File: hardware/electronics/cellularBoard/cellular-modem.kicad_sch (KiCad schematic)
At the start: 24 parts, among them Q1 DMG1013TQ-7, U4 OPA344, U5 SARA-R422S-01B

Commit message: started on schematics
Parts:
- removed U5: SARA-R422S-01B, DSE-RF-Receivers:ZED-F9P-04B_UBL, symbol DS-RF-Tranceivers-and-Modems:SARA-R422S-01B
- added U2: LEXI-R520, symbol lib_sch:LEXI-R520
- added U3: LM51571-Q1, symbol lib_sch:LM51571-Q1
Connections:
- net VCC: now also U2.40 (VCC), U2.41 (VCC), U2.42 (VCC)
- net VSS: now also U2.1 (GND), U2.100 (GND), U2.101 (GND), U2.102 (GND), U2.103 (GND), U2.104 (GND), U2.105 (GND), U2.106 (GND), U2.109 (GND), U2.110 (GND), U2.111 (GND), U2.112 (GND), U2.113 (GND), U2.114 (GND), U2.115 (GND), U2.116 (GND), U2.117 (GND), U2.118 (GND), U2.119 (GND), U2.120 (GND), U2.121 (GND), U2.122 (GND), U2.123 (GND), U2.124 (GND), U2.125 (GND), U2.126 (GND), U2.127 (GND), U2.128 (GND), U2.129 (GND), U2.130 (GND), U2.131 (GND), U2.132 (GND), U2.133 (GND), U2.3 (GND), U2.50 (GND), U2.52 (GND), U2.53 (GND), U2.56 (GND), U2.57 (GND), U2.58 (GND), U2.59 (GND), U2.60 (GND), U2.61 (GND), U2.64 (GND), U2.65 (GND), U2.66 (GND), U2.67 (GND), U2.68 (GND), U2.69 (GND), U2.70 (GND), U2.73 (GND), U2.74 (GND), U2.75 (GND), U2.76 (GND), U2.77 (GND), U2.78 (GND), U2.79 (GND), U2.82 (GND), U2.83 (GND), U2.84 (GND), U2.85 (GND), U2.86 (GND), U2.87 (GND), U2.88 (GND), U2.91 (GND), U2.92 (GND), U2.93 (GND), U2.94 (GND), U2.95 (GND), U2.96 (GND), U2.97 (GND)
- net SARA_D+ renamed LEXI_D+
- net LEXI_D+: now also U2.21 (USB_D+)
- net SARA_D- renamed LEXI_D-
- net LEXI_D-: now also U2.20 (USB_D-)
- new net: U2.107 (RSVD), U2.108 (RSVD), U2.19 (RSVD), U2.23 (RSVD), U2.24 (RSVD), U2.25 (RSVD), U2.26 (RSVD), U2.48 (RSVD), U2.54 (RSVD), U2.55 (RSVD), U2.62 (RSVD), U2.63 (RSVD), U2.71 (RSVD), U2.72 (RSVD), U2.80 (RSVD), U2.81 (RSVD), U2.89 (RSVD), U2.90 (RSVD), U2.98 (RSVD), U2.99 (RSVD)
- new net: U3.1 (PGND), U3.16 (PGND)
- new net: U3.12 (SW), U3.13 (SW), U3.14 (SW)
- new net: U3.17 (AGND), U3.7 (AGND)
- new net +1V8: U2.43 (V_INT)
- new net LEXI_CTS_1V8: U2.6 (CTS)
- new net LEXI_RTS_1V8: U2.7 (RTS)
- new net LEXI_RXD_1V8: U2.4 (RXD)
- new net LEXI_SCL_1V8: U2.12 (SCL)
- new net LEXI_SDA_1V8: U2.13 (SDA)
- new net LEXI_TXD_1V8: U2.5 (TXD)
- no-connect marks 12 -> 10
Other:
- moved on the sheet: AE1, C10, C9, D6, L1, Q1, R10, R11, R12, R13, R15, R16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

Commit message: finished schematic
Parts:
- removed C10: 10nF, lib_fp:MLCC0603, symbol lib_sch:C
- removed C3, C6: 1uF, lib_fp:MLCC0603, symbol lib_sch:C
- removed C4, C5, C7: 100nF, lib_fp:MLCC0603, symbol lib_sch:C
- removed C8: 2.2uF, lib_fp:MLCC0603, symbol lib_sch:C
- removed C9: 47pF, lib_fp:MLCC0603, symbol lib_sch:C_horizontal
- removed L1: 47nH, lib_fp:L_0402, symbol lib_sch:L
- removed Q1: DMG1013TQ-7, lib_fp:SOT23-3P50_160X160X75L22X22N, symbol lib_sch:PMOS_DGS
- removed R10: 10R, lib_fp:CRCW0603, symbol lib_sch:R
- removed R13: 10K, lib_fp:CRCW0402, symbol lib_sch:R_horizontal
- removed R15: 1K, lib_fp:CRCW0402, symbol lib_sch:R
- removed R16: 100K, lib_fp:CRCW0402, symbol lib_sch:R
- removed R8: 10K, lib_fp:CRCW0402, symbol lib_sch:R
- removed TP10, TP11, TP9: ~, lib_fp:TP_1mm, symbol lib_sch:Testpoint
- removed U3: LM51571-Q1, symbol lib_sch:LM51571-Q1
- removed U4: OPA344, lib_fp:SOT23-5P95_280X300X110L40X38N, symbol lib_sch:TS391
- added C12, C13, C14, C15: 47pF, lib_fp:MLCC0603, symbol lib_sch:C
- added C16: 100nF, lib_fp:MLCC0603, symbol lib_sch:C
- added C17: 47pF, lib_fp:MLCC0603, symbol lib_sch:C_horizontal
- added C18: 39pF, lib_fp:MLCC0603, symbol lib_sch:C
- added D4, D5, D7: VAL, lib_fp:SOD882, symbol lib_sch:D_TVS
- added D8: PTVS4V5D1BLYL, lib_fp:SOD882, symbol lib_sch:D_TVS
- added J3: 0786463001, symbol lib_sch:SIM_Card
- added L2: 39nH, symbol lib_sch:L
- added L3: 82nH, symbol lib_sch:L
- added R11: 10K, lib_fp:CRCW0402, symbol lib_sch:R_horizontal
- D6: value PTVS4V5D1BLYL -> VAL; Package SOD-882 -> PKG
- renumbered R12 to R10, R11 to R9
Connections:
- net ANT_DET: now also U2.49 (ANT_DET), R11.1
- net MODULE_STS: now also U2.15 (GPIO2)
- net NETWORK_STS: now also U2.14 (GPIO1)
- net RESET_N: now also U2.28 (RESET_N)
- net RF_IN: now also U2.51 (ANT), C17.1, L2.1
- net VSS: now also C12.2, C13.2, C14.2, C15.2, C16.2, C18.2, D4.1, D5.1, D7.1, D8.1, J3.C4 (GND), J3.MP3 (MP), J3.MP4 (MP), J3.MP5 (MP), J3.MP6 (MP), J3.MP7 (MP), J3.MP8 (MP), L2.2
- net SLEEP: now reaches U2.27 (PWR_ON)
- net SIM_RST: now reaches U2.30 (SIM_RST)
- net SIM_RST: now also D6.2, C14.1, J3.C2 (RST)
- net SIM_CLK: now reaches U2.31 (SIM_CLK)
- net SIM_CLK: now also C13.1, D5.2, J3.C3 (CLK)
- net SIM_IO: now reaches U2.32 (SIM_IO)
- net SIM_IO: now also C12.1, D4.2, J3.C6 (SDIO)
- net VSIM: now reaches U2.33 (VSIM)
- net VSIM: now also C15.1, C16.1, D7.2, J3.C1 (VCC)
- net ANT_IN: no longer names the net of AE1.1 (A)
- net ANT_IN: now also C17.2, L3.1; no longer D6.2
- net VCC renamed +3V8
- new net: J3.MP1 (NC), J3.MP2 (NC)
- new net: C18.1, D8.2, L3.2, R11.2
- no-connect marks 10 -> 21

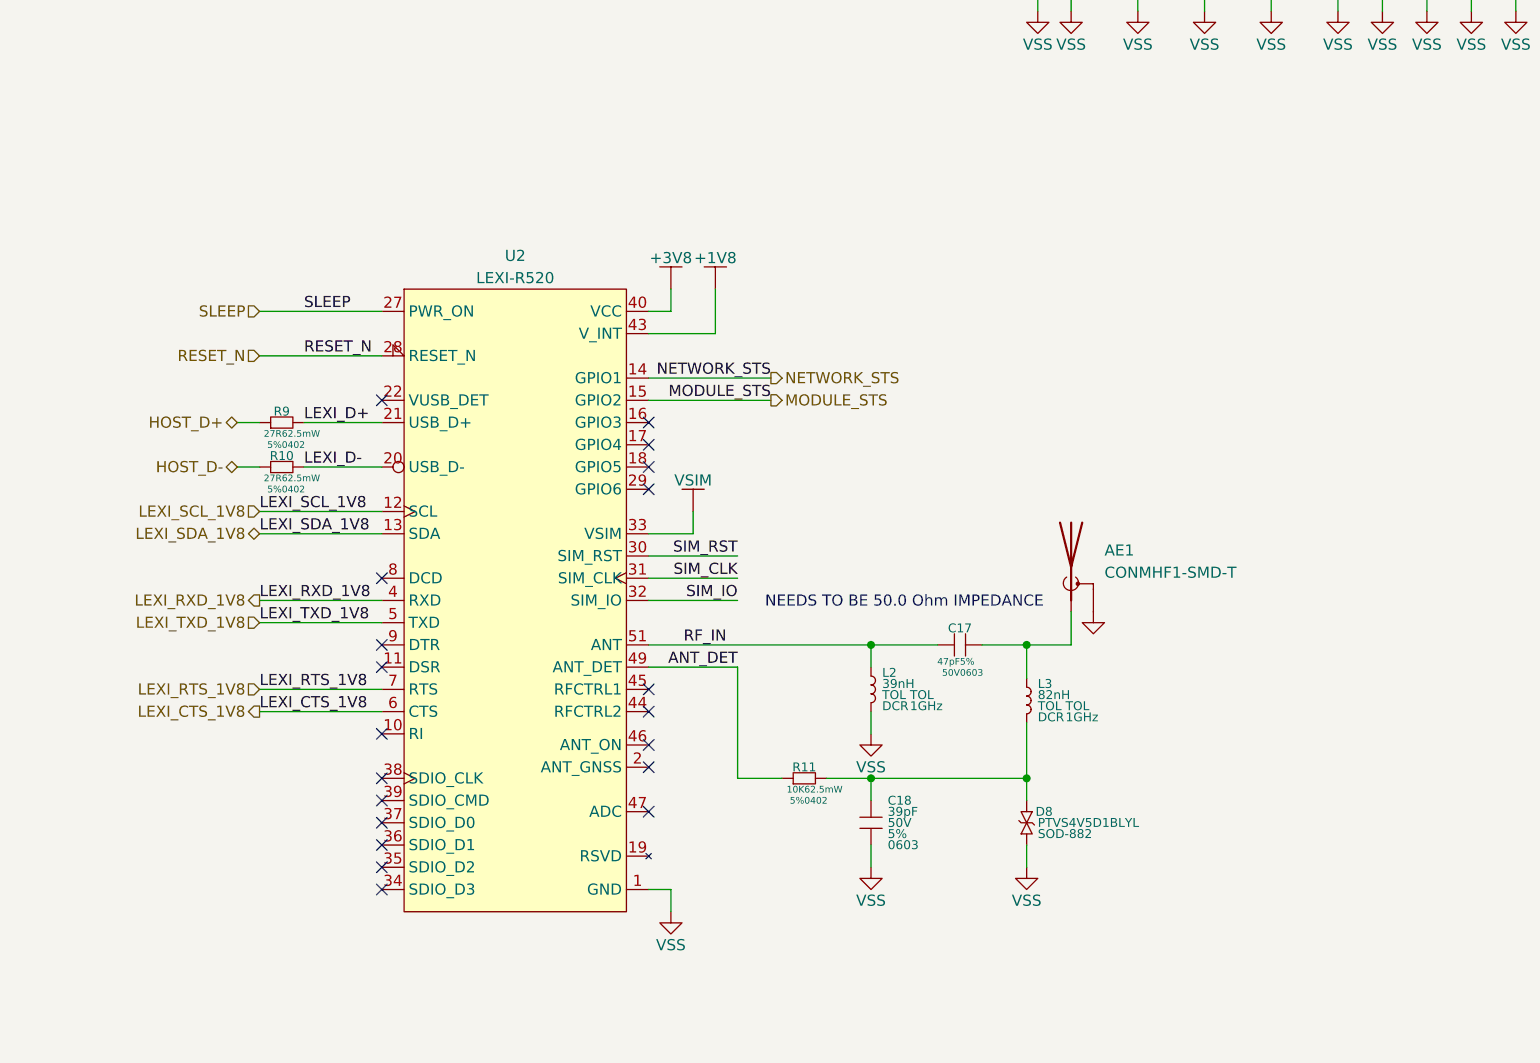
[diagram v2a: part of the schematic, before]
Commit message: replaced LEXI-R52 with SARA-R52
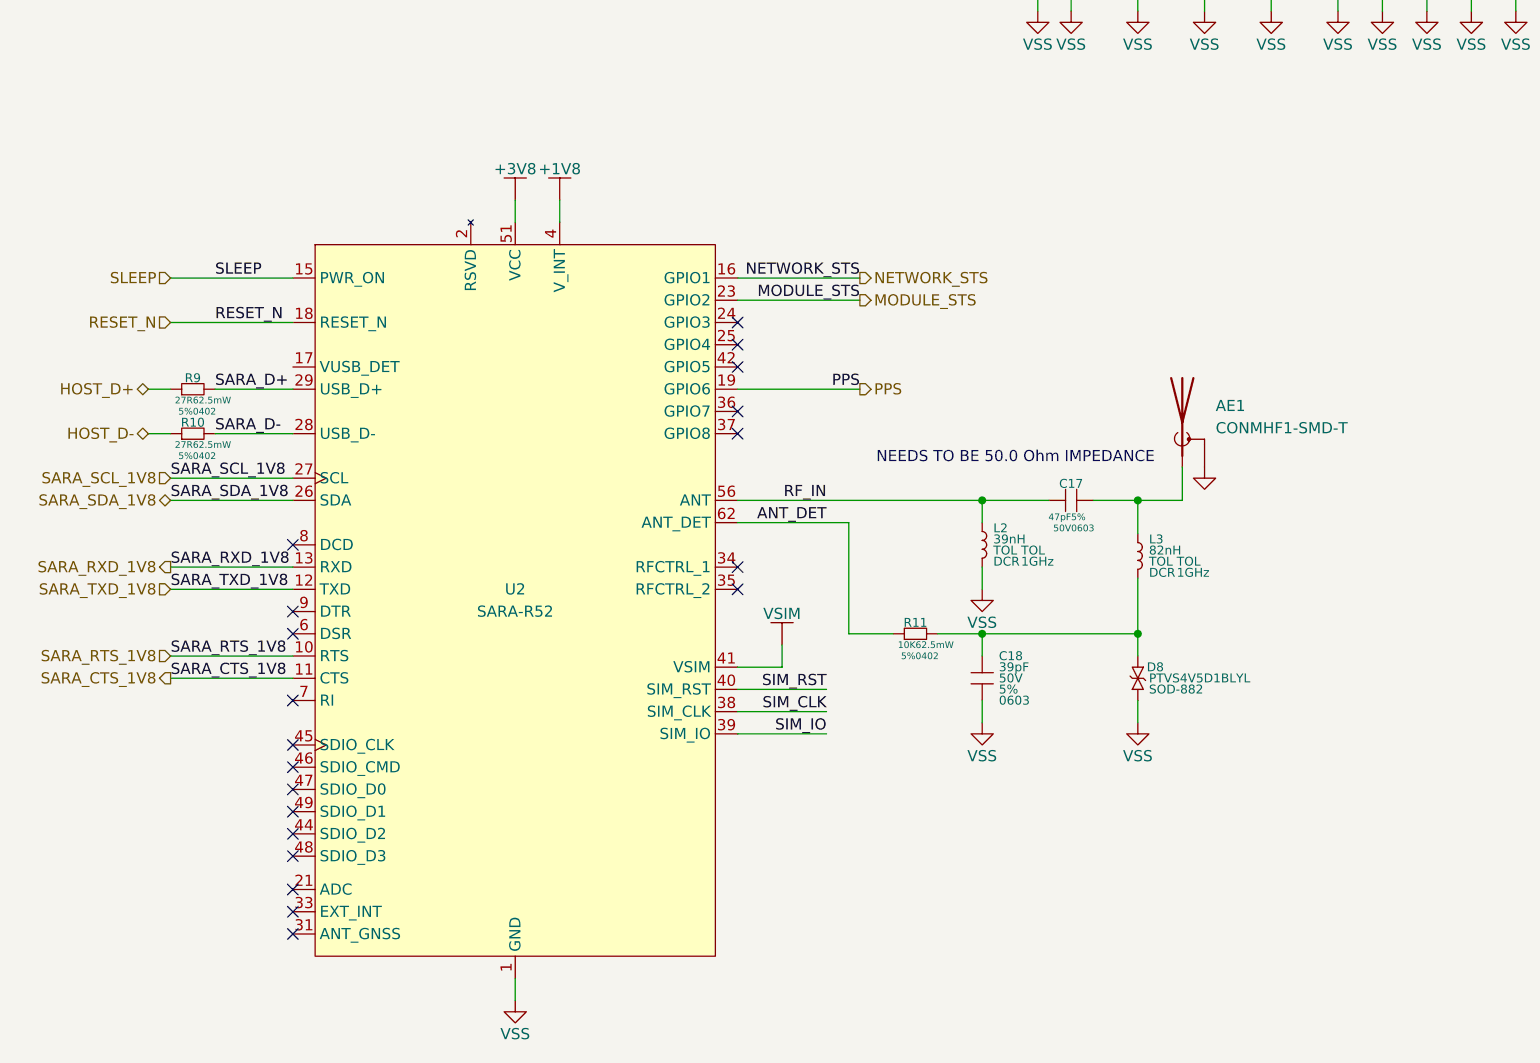
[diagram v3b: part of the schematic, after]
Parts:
- removed U2: LEXI-R520, symbol lib_sch:LEXI-R520
- added U2: SARA-R52, DSE-RF-Receivers:ZED-F9P-04B_UBL, symbol DS-RF-Tranceivers-and-Modems:SARA-R52
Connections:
- net +1V8: now also U2.4 (V_INT)
- net +3V8: now also U2.51 (VCC), U2.52 (VCC), U2.53 (VCC)
- net ANT_DET: now also U2.62 (ANT_DET)
- net MODULE_STS: now also U2.23 (GPIO2)
- net NETWORK_STS: now also U2.16 (GPIO1)
- net RESET_N: now also U2.18 (RESET_N)
- net RF_IN: now also U2.56 (ANT)
- net SIM_CLK: now also U2.38 (SIM_CLK)
- net SIM_IO: now also U2.39 (SIM_IO)
- net SIM_RST: now also U2.40 (SIM_RST)
- net SLEEP: now also U2.15 (PWR_ON)
- net VSIM: now also U2.41 (VSIM)
- net VSS: now also U2.1 (GND), U2.14 (GND), U2.20 (GND), U2.22 (GND), U2.3 (GND), U2.30 (GND), U2.32 (GND), U2.43 (GND), U2.5 (GND), U2.50 (GND), U2.54 (GND), U2.55 (GND), U2.57 (GND), U2.58 (GND), U2.59 (GND), U2.60 (GND), U2.61 (GND), U2.63 (GND), U2.64 (GND), U2.65 (GND), U2.66 (GND), U2.67 (GND), U2.68 (GND), U2.69 (GND), U2.70 (GND), U2.71 (GND), U2.72 (GND), U2.73 (GND), U2.74 (GND), U2.75 (GND), U2.76 (GND), U2.77 (GND), U2.78 (GND), U2.79 (GND), U2.80 (GND), U2.81 (GND), U2.82 (GND), U2.83 (GND), U2.84 (GND), U2.85 (GND), U2.86 (GND), U2.87 (GND), U2.88 (GND), U2.89 (GND), U2.90 (GND), U2.91 (GND), U2.92 (GND), U2.93 (GND), U2.94 (GND), U2.95 (GND), U2.96 (GND)
- net LEXI_D+ renamed SARA_D+
- net SARA_D+: now also U2.29 (USB_D+)
- net LEXI_D- renamed SARA_D-
- net SARA_D-: now also U2.28 (USB_D-)
- new net PPS: U2.19 (GPIO6)
- new net SARA_CTS_1V8: U2.11 (CTS)
- new net SARA_RTS_1V8: U2.10 (RTS)
- new net SARA_RXD_1V8: U2.13 (RXD)
- new net SARA_SCL_1V8: U2.27 (SCL)
- new net SARA_SDA_1V8: U2.26 (SDA)
- new net SARA_TXD_1V8: U2.12 (TXD)
